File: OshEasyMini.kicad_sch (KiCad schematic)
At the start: 120 parts, among them J1 TAGCONNECT, J10 Conn_01x04_MountingPin, J2 Screw_Terminal_01x06, J3 SMA_Edgelaunch, J4 Conn_01x02_MountingPin, J5 UFL, J6 Conn_01x05, J7 Conn_01x06, J8 Conn_01x02, Q1 SiA449DJ, Q2 AO3400A, Q3 SiA449DJ, U11 CPT-7502-65-SMT-TR, U12 LM293QT, U17 MCP73831-2-OT, U18 TC2185-3.3VxCTTR, U19 W25Q64JVXGIQ, U2 WE-TVS-82400102, U20 SISB46DN, U21 SN74LVC1G80QDCKTQ1, U3 ADXL375, U4 MS5607-02BA, U5 MAX-M10S, U6 MCP130-xxxxTT, U7 DRV5012AEDMRR, U8 CC1200, U9 ATSAMD21G17D-A, X2 ECS-160-8-36Q-AES-TR1, Y1 ABM8W-40.0000MHZ

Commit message: good progress, changed to mia-m10
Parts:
- removed C11, C12, C14, C15, C28: 47nF, Capacitor_SMD:C_0402_1005Metric, symbol Device:C
- removed J2: Screw_Terminal_01x06, symbol Connector:Screw_Terminal_01x06
- removed J4: Conn_01x02_MountingPin, Connector_JST:JST_PH_S2B-PH-SM4-TB_1x02-1MP_P2.00mm_Horizontal, symbol Connector_Generic_MountingPin:Conn_01x02_MountingPin
- removed J6: Conn_01x05, Connector_PinHeader_2.54mm:PinHeader_1x05_P2.54mm_Vertical, symbol Connector_Generic:Conn_01x05
- removed J7: Conn_01x06, Connector_PinHeader_2.54mm:PinHeader_1x06_P2.54mm_Vertical, symbol Connector_Generic:Conn_01x06
- removed J8: Conn_01x02, Connector_PinHeader_2.54mm:PinHeader_1x02_P2.54mm_Vertical, symbol Connector_Generic:Conn_01x02
- removed R38, R39: 1k, Resistor_SMD:R_0402_1005Metric, symbol Device:R
- removed U5: MAX-M10S, RF_GPS:ublox_MAX, symbol RF_GPS:MAX-M10S
- added C47, C48, C49, C50, C51: 47nF, Capacitor_SMD:C_0201_0603Metric, symbol Device:C
- added C52: 47pF, Capacitor_SMD:C_0402_1005Metric, symbol Device:C
- added FL1: SAFFB1G58KA0F0A, Filter:Filter_1109-5_1.1x0.9mm, symbol Filter:SAFFB1G58KA0F0A
- added J2: Screw_Terminal_01x03, FCU2025Lib:Horizontal2.5mmWago3pin, symbol Connector:Screw_Terminal_01x03
- added J6: Conn_01x02, Connector_JST:JST_PH_S2B-PH-K_1x02_P2.00mm_Horizontal, symbol Connector_Generic:Conn_01x02
- added R55: 100k, Resistor_SMD:R_0201_0603Metric, symbol Device:R
- added R57, R58: 0, Resistor_SMD:R_0201_0603Metric, symbol Device:R
- added R59: 1k, Resistor_SMD:R_0201_0603Metric, symbol Device:R
- added U1: MIA-M10Q, Package_LGA:ublox_LGA-53_4.5x4.5mm_Layout9x9_P0.5mm, symbol RF_GPS:MIA-M10Q
- added Y2: 32.768khz, Crystal:Crystal_SMD_2012-2Pin_2.0x1.2mm, symbol Device:Crystal
- C29, C30, C32, C34: footprint Capacitor_SMD:C_0402_1005Metric -> Capacitor_SMD:C_0201_0603Metric
- R11, R50, R51, R53, R56: footprint Resistor_SMD:R_0402_1005Metric -> Resistor_SMD:R_0201_0603Metric
- R52: value 100k -> 1k; footprint Resistor_SMD:R_0402_1005Metric -> Resistor_SMD:R_0201_0603Metric
- Y1: value ABM8W-40.0000MHZ -> 40mhz 8pF 30 Ohms; footprint Crystal:Crystal_SMD_Abracon_ABM8G-4Pin_3.2x2.5mm -> Crystal:Crystal_SMD_Abracon_ABM10-4Pin_2.5x2.0mm
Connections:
- net +3V3: now also C32.2, C34.2, C47.2, C48.2, C49.2, U1.B1 (VCC), U1.J4 (V_IO)
- net FET_A: now also J2.3 (Pin_3)
- net FET_B: now also J2.2 (Pin_2)
- net GND: now also R52.2, C47.1, C48.1, C49.1, C50.1, C51.1, FL1.2, FL1.3, FL1.5, J6.2 (Pin_2), R55.1, R57.2, R58.2, U1.A1 (GND), U1.A2 (GND), U1.A3 (GND), U1.A8 (GND), U1.A9 (GND), U1.B2 (GND), U1.B8 (GND), U1.C3 (GND), U1.C9 (GND), U1.E3 (GND), U1.E4 (GND), U1.E9 (GND), U1.F1 (GND), U1.F3 (GND), U1.F4 (GND), U1.G3 (GND), U1.G4 (GND), U1.G5 (GND), U1.G6 (GND), U1.H8 (GND), U1.J8 (GND), U1.J9 (GND); no longer R52.1
- net NRST: now also U1.C4 (~{RESET})
- net RX1: now also U1.H1 (RX)
- net TX1: now also U1.G1 (TX)
- net VBUS: now also R59.2
- net V_CHARGE: now also J6.1 (Pin_1)
- net V_LIPO: now also J2.1 (Pin_1)
- net at D4.2 (A2): now also R59.1
- net at D4.3 (K1): now also R52.1
- net at FB2.1, J5.1 (In): now also C52.1
- net at R54.1: now also U1.C6 (VCC_RF)
- net at D6.2 (A): now also U1.A7 (TIMEPULSE)
- net at R11.1: now also U1.J5 (V_BCKP)
- net at D5.1 (A1), D5.2 (A2), R50.1: now also R51.2; no longer R51.1
- net at D2.2, U21.1 (D), U21.4 (~{Q}): now also R51.1; no longer R51.2
- net at D2.3, JP1.1 (A), Q2.1 (G): now also R55.2; no longer R52.2
- net at U8.29 (DCPL_XOSC): now also C50.2; no longer C34.2
- net at U8.26 (DCPL_PFD_CHP): now also C51.2; no longer C32.2
- new net: C52.2, FL1.4
- new net: U1.A4 (RTC_I), Y2.2
- new net: U1.A5 (RTC_O), Y2.1
- new net: FL1.1, U1.B9 (RF_IN)
- new net: R57.1, U1.F9 (Reserved)
- new net: R58.1, U1.G7 (Reserved)
- no-connect marks 12 -> 15
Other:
- moved on the sheet: C43, D6, FB2, J5, R11, R54, R56

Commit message: all components placed currently routing
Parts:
- removed J2: Screw_Terminal_01x03, FCU2025Lib:Horizontal2.5mmWago3pin, symbol Connector:Screw_Terminal_01x03
- removed R10: 22, Resistor_SMD:R_0402_1005Metric, symbol Device:R
- removed R4: 1k, Resistor_SMD:R_0402_1005Metric, symbol Device:R
- added J4: Screw_Terminal_01x03, TerminalBlock_Phoenix:TerminalBlock_Phoenix_MPT-0,5-3-2.54_1x03_P2.54mm_Horizontal, symbol Connector:Screw_Terminal_01x03
- added JP2: SolderJumper_2_Open, Jumper:SolderJumper-2_P1.3mm_Open_TrianglePad1.0x1.5mm, symbol Jumper:SolderJumper_2_Open
- added R1: 22, Resistor_SMD:R_0201_0603Metric, symbol Device:R
- added R2: 1k, Resistor_SMD:R_0201_0603Metric, symbol Device:R
- C22: footprint Capacitor_SMD:C_0402_1005Metric -> Capacitor_SMD:C_0201_0603Metric
- J10: footprint Connector_JST:JST_SH_SM04B-SRSS-TB_1x04-1MP_P1.00mm_Horizontal -> Connector_JST:JST_SH_BM04B-SRSS-TB_1x04-1MP_P1.00mm_Vertical
- J6: footprint Connector_JST:JST_PH_S2B-PH-K_1x02_P2.00mm_Horizontal -> Connector_JST:JST_PH_B2B-PH-K_1x02_P2.00mm_Vertical
- JP1: footprint Jumper:SolderJumper-2_P1.3mm_Open_RoundedPad1.0x1.5mm -> Jumper:SolderJumper-2_P1.3mm_Open_TrianglePad1.0x1.5mm
- R3, R40, R41, R42, R43, R46, R47, R49, R9: footprint Resistor_SMD:R_0402_1005Metric -> Resistor_SMD:R_0201_0603Metric
- Y2: footprint Crystal:Crystal_SMD_2012-2Pin_2.0x1.2mm -> Crystal:Crystal_SMD_MicroCrystal_CM9V-T1A-2Pin_1.6x1.0mm
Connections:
- net V_PROT is gone; now on net MGSW_IN: Q1.4 (S)
- net CS_COMP0: now also JP2.2 (B)
- net FET_A: now also J4.2 (Pin_2)
- net FET_B: now also J4.1 (Pin_1)
- net GND: now also JP2.1 (A)
- net V_LIPO: now also J4.3 (Pin_3)
- net at U9.20 (PB11): now also R2.2
- net at U2.3: now also R1.2
- net at D5.2 (A2), R51.2: no longer D5.1 (A1), R50.1
- net at D3.2 (A2): now also R2.1
- net at J10.1 (Pin_1): now also R1.1
- new net: D5.1 (A1), R50.1
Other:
- moved on the sheet: C43, C52, D5, D6, FB2, FL1, J5, J6, R11, R50, R51, R54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

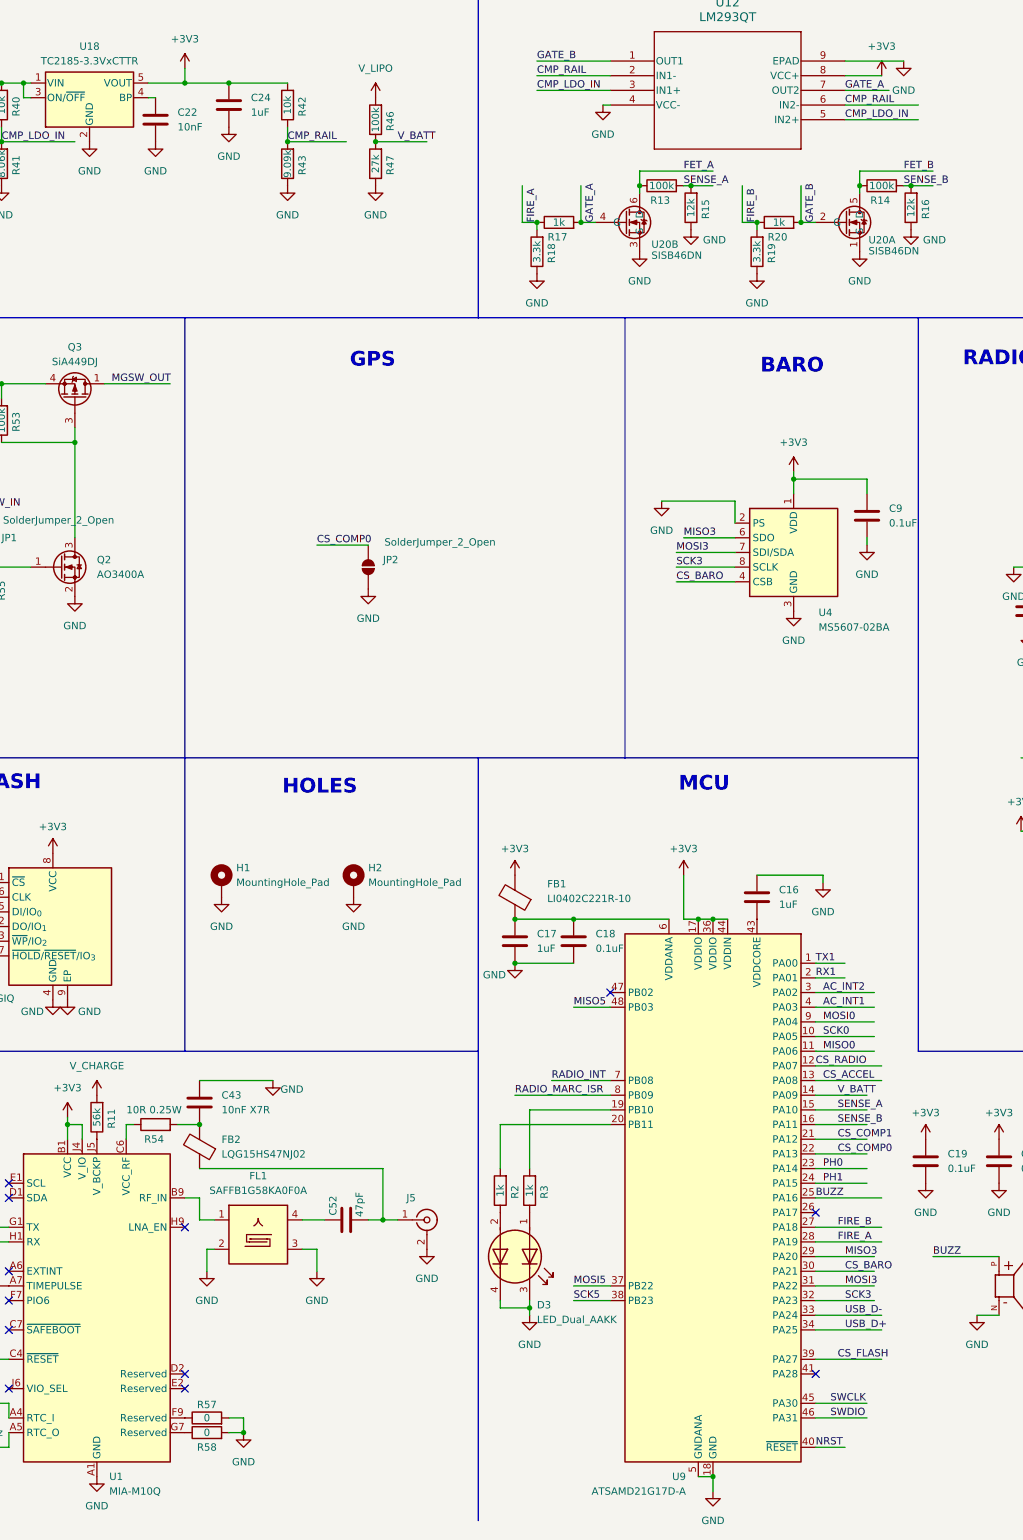
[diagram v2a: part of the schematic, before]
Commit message: routing done, need to remove SAW and impedance match
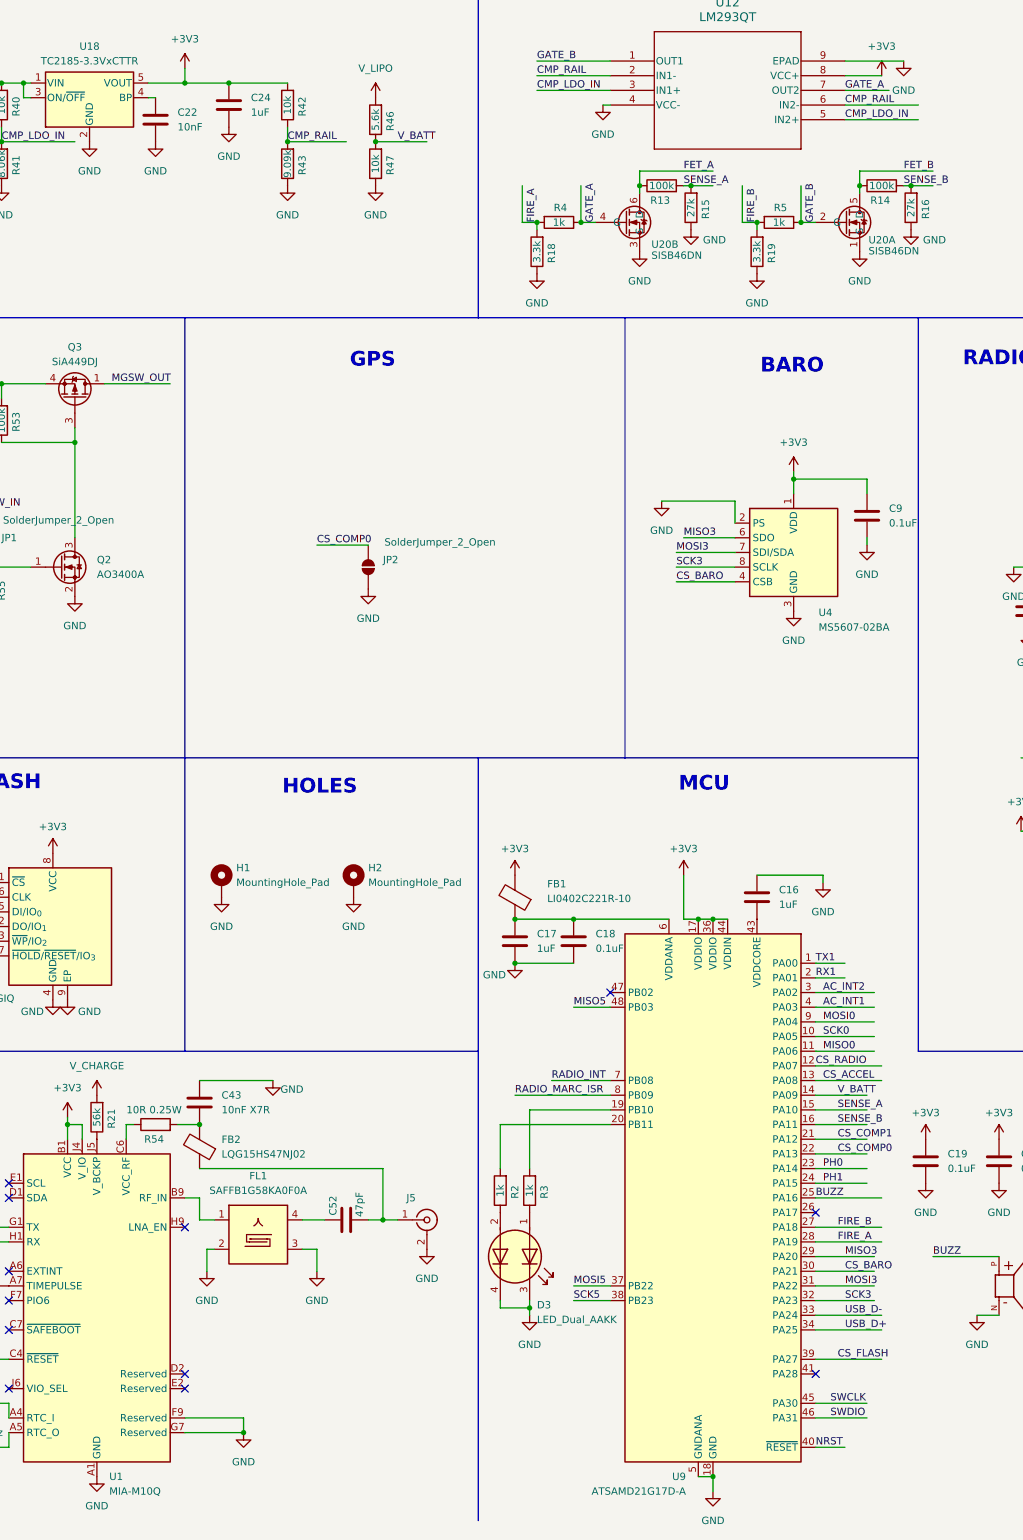
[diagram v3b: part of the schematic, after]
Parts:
- removed R11: 56k, Resistor_SMD:R_0201_0603Metric, symbol Device:R
- removed R17, R20: 1k, Resistor_SMD:R_0402_1005Metric, symbol Device:R
- removed R57, R58: 0, Resistor_SMD:R_0201_0603Metric, symbol Device:R
- added R21: 56k, Resistor_SMD:R_0402_1005Metric, symbol Device:R
- added R4, R5: 1k, Resistor_SMD:R_0201_0603Metric, symbol Device:R
- R15, R16: value 12k -> 27k
- R46: value 100k -> 5.6k
- R47: value 27k -> 10k
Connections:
- net FIRE_A: now also R4.2
- net FIRE_B: now also R5.2
- net GATE_A: now also R4.1
- net GATE_B: now also R5.1
- net GND: now also U1.F9 (Reserved), U1.G7 (Reserved)
- net V_CHARGE: now also R21.2
- net at U1.J5 (V_BCKP): now also R21.1
